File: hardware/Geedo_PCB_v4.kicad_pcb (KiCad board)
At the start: 2 copper layers, 29.5 x 51.5 mm, 25 parts, among them J1 USB-C, J2 BATTERY, J3 OLED, SW1 MAIN_BTN, SW2 BOOT_BTN, SW3 RESET_BTN, U1 MCP73831, U2 MCP1826S-3302, U3 ESP32-C3-MINI-1

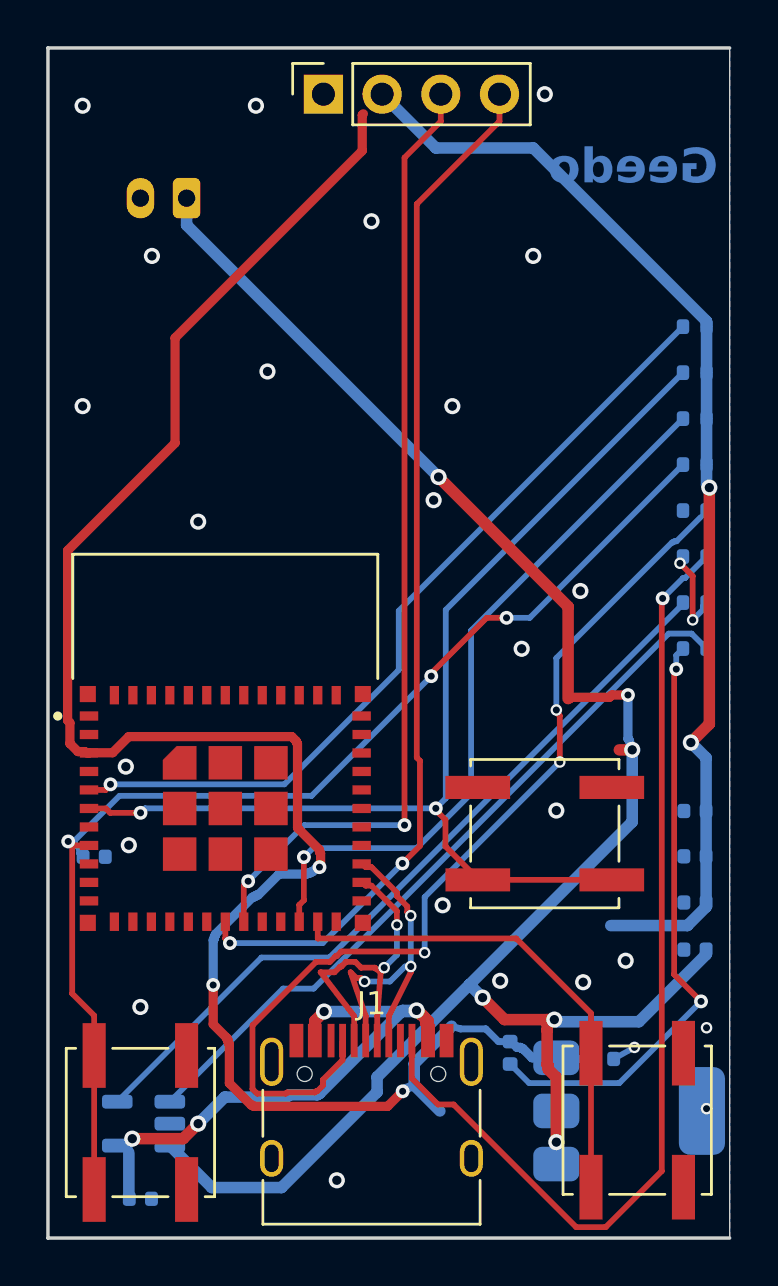
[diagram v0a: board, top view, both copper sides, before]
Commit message: pcb: reconnect the 3.3 V rail and clear the DRC errors
KiCad's DRC found things my offline checks were blind to. The important one:

+3V3 was in two electrically separate islands. One held U3.3, U2.3, C6.1
and D1.2; the other held J3.2 (the OLED header's 3.3 V pin) and every
pull-up on the board - R1, R2, R3, R8 - plus C2, C3 and C4. The regulator
output never reached any of them, so the IO2 and IO8 straps the ESP32-C3
needs held high to boot had no supply. The board would not have started.

The routing had stopped 1.2 mm short: a front-side stub dead-ending at
(103.15, 77.85) and a back-side track dead-ending at (103.96, 77.00), on
opposite layers with nothing between them. Joined with a via at the
front-side tip and a back-side track across the gap.

Also from the report:

- C6 sat underneath U2's SOT-223 body - I had placed it 2 mm from the
  regulator output but on the wrong side of it, which is not assemblable.
  Moved to (110.30, 115.80) rotated 180, outside every courtyard, with
  3.3 V re-routed to U2.3 in four segments that jog around the VBAT via.
  Four stale copper items from the old position ripped.
- The "Geedo" copper lettering overlapped a +3V3 track. Moved to
  (112.55, 87.30), clear of copper and of the antenna keepout.
- U2's thermal tab was 0.2 mm from the board outline where the setup asks
  0.5 mm. U2 moved to (114.30, 120.90); that clipped D1's courtyard by
  0.07 mm, so D1 moved to (109.30, 118.535). Tab is now 0.55 mm off the
  edge with 0.22 mm to the nearest copper.
- A ground stitching via sat inside U2's tab. Via-in-pad wicks solder off
  the joint during reflow, so it moved from (118.0, 120.9) to (118.0, 124.2),
  past the end of the tab.
- Pruned three dangling track stubs. A fourth, on CC1, turned out not to be
  a leaf - removing it split the net - so it stays.

Two blind spots fixed in tools/drc_offline.py that let the above through:
copper text was modelled as centred on its anchor when a justified, mirrored
string is anchored by a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
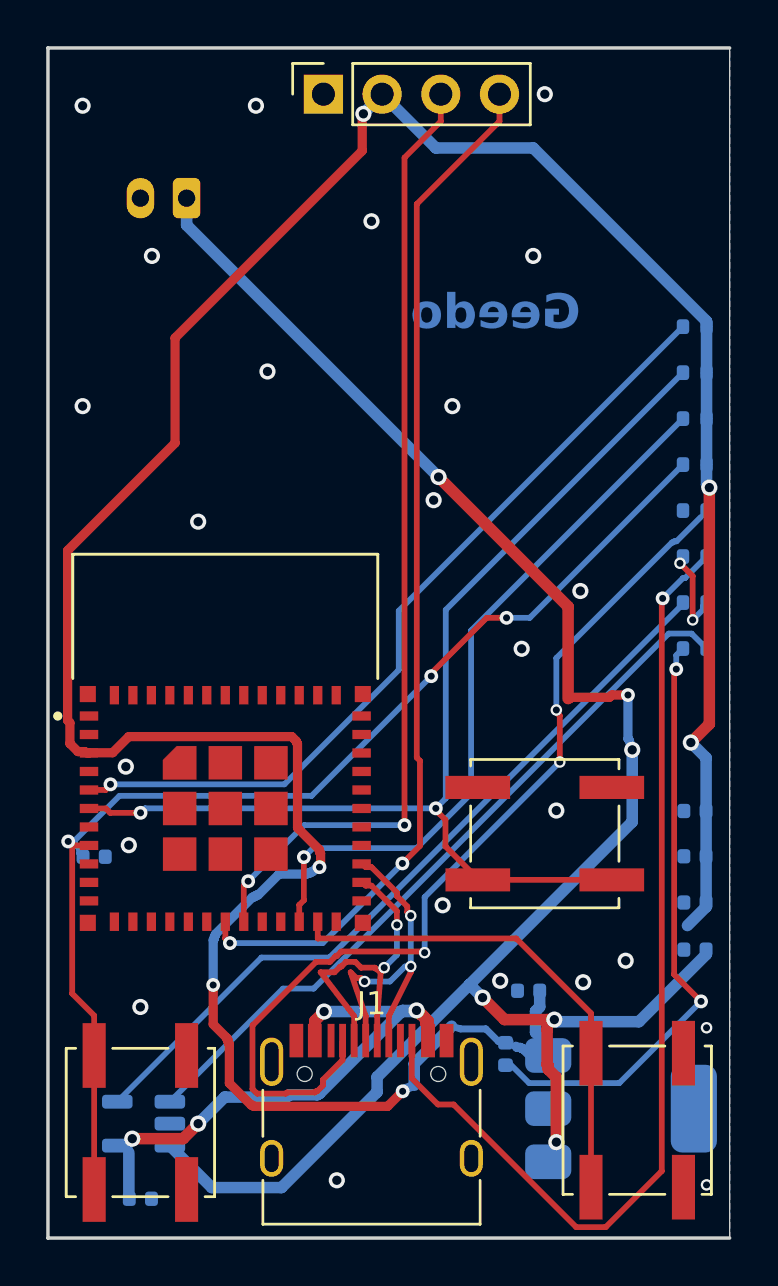
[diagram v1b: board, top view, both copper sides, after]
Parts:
- moved C6 4.35 mm to (110.3, 115.8), turned to 180 degrees
- moved U2 0.36 mm to (114.3, 120.9)
- moved D1 0.21 mm to (109.3, 118.5)
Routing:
- net +3V3: track 128.7 -> 127.1 mm, vias 5 -> 6
- net GND: track 4.71 -> 3.68 mm, vias 27 -> 26
- net /VBAT: track 83.7 -> 83.1 mm
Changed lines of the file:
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@@
 	(footprint "Capacitor_SMD:C_0402_1005Metric"
 		(layer "B.Cu")
-		(at 113.5 118.75)
+		(at 110.3 115.8 180)
 		(descr "Capacitor SMD 0402 (1005 Metric), square (rectangular) end terminal, IPC_7351 nominal, (Body size source: IPC-SM-782 page 76, https://www.pcb-3d.com/wordpress/wp-content/uploads/ipc-sm-782a_amendment_1_and_2.pdf), generated with kicad-footprint-generator")
 		(tags "capacitor")
@@
 	(footprint "Package_TO_SOT_SMD:SOT-223-3_TabPin2"
 		(layer "B.Cu")
-		(at 114.65 121)
+		(at 114.3 120.9)
 		(descr "module CMS SOT223 4 pins")
 		(tags "CMS SOT")
@@
 	(footprint "LED_SMD:LED_0402_1005Metric"
 		(layer "B.Cu")
-		(at 109.5 118.485 90)
+		(at 109.3 118.535 90)
 		(descr "LED SMD 0402 (1005 Metric), square (rectangular) end terminal, IPC_7351 nominal, (Body size source: http://www.tortai-tech.com/upload/download/2011102023233369053.pdf), generated with kicad-footprint-generator")
 		(tags "LED")
@@
 	)
 	(gr_text "Geedo"
-		(at 118.5 81 -0)
+		(at 112.55 87.3 -0)
 		(layer "B.Cu")
 		(effects
@@
 	)
 	(segment
-		(start 114.2259 105.3744)
-		(end 114.784 105.3744)
-		(width 0.5)
-		(layer "F.Cu")
-		(net 1)
-	)
-	(segment
 		(start 111.1 117.5)
 		(end 111.1 117.047)
@@
 	)
 	(segment
-		(start 117.1726 112.9782)
-		(end 113.8544 112.9782)
-		(width 0.5)
-		(layer "B.Cu")
-		(net 3)
-	)
-	(segment
 		(start 96.75 113.4)
 		(end 96.7 113.45)
@@
 	)
 	(segment
-		(start 105.3502 119.8887)
-		(end 106.4615 121)
-		(width 0.5)
-		(layer "B.Cu")
-		(net 3)
-	)
-	(segment
 		(start 116.5972 115.095)
 		(end 117.7614 116.2592)
@@
 	)
 	(via
-		(at 114.88 118.25)
-		(size 0.5)
-		(drill 0.3)
+		(at 103.15 77.85)
+		(size 0.7)
+		(drill 0.4)
 		(layers "F.Cu" "B.Cu")
-		(net 2)
+		(net 3)
 	)
-	(via
-		(at 118.0 120.9)
-		(size 0.5)
-		(drill 0.3)
-		(layers "F.Cu" "B.Cu")
-		(net 2)
+	(segment
+		(start 103.15 77.85)
+		(end 103.96 77.0)
+		(width 0.5)
+		(layer "B.Cu")
+		(net 3)
 	)
-	(via
-		(at 118.0 117.4)
-		(size 0.5)
-		(drill 0.3)
-		(layers "F.Cu" "B.Cu")
-		(net 2)
+	(segment
+		(start 110.78 115.8)
+		(end 110.78 116.5)
+		(width 0.5)
+		(layer "B.Cu")
+		(net 3)
 	)
 	(segment
-		(start 113.02 118.75)
-		(end 113.0 118.75)
-		(width 0.3)
+		(start 110.78 116.5)
+		(end 110.6 116.68)
+		(width 0.5)
 		(layer "B.Cu")
 		(net 3)
 	)
 	(segment
-		(start 113.0 118.75)
-		(end 112.5 118.75)
-		(width 0.3)
+		(start 110.6 116.68)
+		(end 110.6 117.6)
+		(width 0.5)
 		(layer "B.Cu")
 		(net 3)
 	)
 	(segment
-		(start 113.98 118.75)
-		(end 114.88 118.25)
-		(width 0.25)
+		(start 110.6 117.6)
+		(end 111.1 118.1)
+		(width 0.5)
 		(layer "B.Cu")
+		(net 3)
+	)
+	(via
+		(at 118.0 124.2)
+		(size 0.5)
+		(drill 0.3)
+		(layers "F.Cu" "B.Cu")
+		(net 2)
+	)
+	(via
+		(at 118.0 117.4)
+		(size 0.5)
+		(drill 0.3)
+		(layers "F.Cu" "B.Cu")
 		(net 2)
 	)

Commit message: pcb: make the logo actually print, as silkscreen artwork
The face logo was a KiCad reference image - an (image ...) element with a
1254x1254 PNG embedded as base64. Reference images are editor-only aids for
tracing and alignment; KiCad never plots them to Gerbers, so the logo had
never reached the fab on any board built from these files.

It was also unprintably small. The PNG is 96% whitespace padding, so at the
stored scale of 0.035834 the face itself came out 2.3 mm wide with 0.18 mm
strokes - at the silkscreen minimum, patchy even if it had plotted.

Trace the bitmap into outlines and store them as a footprint, Geedo:Logo, of
fp_poly shapes on F.SilkS. Same position as before, (115.5, 77), sized so the
face is 6.0 x 3.19 mm with 0.47 mm strokes. Contours come from marching
squares over a smoothed, downsampled mask, simplified with Douglas-Peucker at
0.012 mm. The mouth's enclosed hole is preserved by fracturing it into the
outer contour with a zero-width slit, the same way KiCad's own bitmap
converter does it.

Drop the reference image: it plotted nothing, sat on top of the new artwork
in the editor, and was 912 kB of base64 in a 1.1 MB board file, now 205 kB.
The source bitmap is kept as hardware/geedo-logo.png.

Artwork lands 0.40 mm inside the board outline and 1.28 mm from the nearest
pad or via. Gates unchanged: clearance 0, keepout 0, edge 4, nets split 0,
netlist 29/29 consistent, ground one piece.

Co-Authored-By: Claude Fable 5 <noreply@anthropic.com>
Claude-Session: https://claude.ai/code/session_011AnT632DFTLYxaJBrifUnG
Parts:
- added LOGO1: Geedo, Geedo:Logo, F.Cu at (115.5, 77.0)

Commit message: pcb: drop the copper lettering, nudge the logo off the top edge
The board carries its name in the silkscreen logo now, so the "Geedo"
copper text on B.Cu is redundant. Deleting it also removes a piece of
unconnected copper sitting inside the ground pour - it was the thing that
a 3.3 V track had been shorting into before it was moved.

Logo moved from (115.5, 77) to (115.5, 77.5). It was 0.40 mm inside the
top outline, which is buildable but tight for silkscreen; it is now
0.90 mm in, and 1.16 mm from the nearest pad.

Gates: clearance 0, keepout 0, edge 4, nets split 0, netlist 29/29
consistent, ground one piece with every pad on poured copper.

Co-Authored-By: Claude Fable 5 <noreply@anthropic.com>
Claude-Session: https://claude.ai/code/session_011AnT632DFTLYxaJBrifUnG
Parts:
- moved LOGO1 0.50 mm to (115.5, 77.5)
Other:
- board text removed: "Geedo"
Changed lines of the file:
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@@
 	(footprint "Geedo:Logo"
 		(layer "F.Cu")
-		(at 115.5 77.0)
+		(at 115.5 77.5)
 		(descr "Geedo face logo, silkscreen artwork traced from the reference bitmap")
 		(attr board_only exclude_from_pos_files exclude_from_bom)
@@
 		(layer "Edge.Cuts")
 	)
-	(gr_text "Geedo"
-		(at 112.55 87.3 -0)
-		(layer "B.Cu")
-		(effects
-			(font
-				(size 1.5 1.5)
-				(thickness 0.3)
-				(bold yes)
-			)
-			(justify left bottom mirror)
-		)
-	)
 	(segment

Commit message: pcb: clear the remaining DRC warnings
The report came back with 0 unconnected pads - the 3.3 V rail is whole.
Clearing what was left:

- Removed the /VBAT via at (114.784, 105.374). It was reported as connected
  on only one layer, which it was: its front-side stub had been pruned
  earlier, and the four back-side tracks meeting there already join
  end-to-end without it.
- Removed two +3V3 stubs at the C2 end, left over from pruning a 3.3 mm
  dead end. Deleting the first exposed the second, so both go.
- Normalised C5 and C7 pad angles from 180 to 0. Both footprints sit at
  rotation 0, so an absolute pad angle of 180 reads as differing from the
  library copy. The pads are symmetric roundrects, so 180 and 0 are the
  same shape and nothing moves - C6 stopped reporting once its footprint
  rotation and pad angles agreed, which is what pointed at this.
- Added hardware/Geedo.pretty/Logo.kicad_mod and hardware/fp-lib-table so
  the Geedo:Logo footprint resolves to a real library instead of reporting
  a missing one, and so the logo can be reused.

What should remain is three copper_edge_clearance errors on the CC2 trace,
which cannot be fixed without moving SW2, and one lib_footprint_mismatch on
U3, whose ESP32 footprint is custom and will always differ from the library.

Gates: clearance 0, keepout 0, edge 4, nets split 0, netlist 29/29
consistent, ground one piece with every pad on poured copper.

Co-Authored-By: Claude Fable 5 <noreply@anthropic.com>
Claude-Session: https://claude.ai/code/session_011AnT632DFTLYxaJBrifUnG
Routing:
- net +3V3: track 127.1 -> 125.8 mm
- net /VBAT: vias 6 -> 5
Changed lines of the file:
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@@
 		)
 		(pad "1" smd roundrect
-			(at -0.48 0 180)
+			(at -0.48 0)
 			(size 0.56 0.62)
 			(layers "B.Cu" "B.Paste" "B.Mask")
@@
 		)
 		(pad "2" smd roundrect
-			(at 0.48 0 180)
+			(at 0.48 0)
 			(size 0.56 0.62)
 			(layers "B.Cu" "B.Paste" "B.Mask")
@@
 		)
 		(pad "1" smd roundrect
-			(at -0.48 0 180)
+			(at -0.48 0)
 			(size 0.56 0.62)
 			(layers "B.Cu" "B.Paste" "B.Mask")
@@
 		)
 		(pad "2" smd roundrect
-			(at 0.48 0 180)
+			(at 0.48 0)
 			(size 0.56 0.62)
 			(layers "B.Cu" "B.Paste" "B.Mask")
@@
 	)
 	(via
-		(at 114.784 105.3744)
-		(size 0.7)
-		(drill 0.4)
-		(layers "F.Cu" "B.Cu")
-		(net 1)
-	)
-	(via
 		(at 106.4027 93.5685)
 		(size 0.7)
@@
 	)
 	(segment
-		(start 117.98 112.1708)
-		(end 117.1726 112.9782)
-		(width 0.5)
-		(layer "B.Cu")
-		(net 3)
-	)
-	(segment
 		(start 118 93.9047)
 		(end 118 93.03)
@@
 		(width 0.5)
 		(layer "B.Cu")
-		(net 3)
-	)
-	(segment
-		(start 117.98 111.98)
-		(end 117.98 112.1708)
-		(width 0.5)
-		(layer "B.Cu")
